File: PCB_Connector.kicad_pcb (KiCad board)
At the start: 2 copper layers, 74.4 x 55.5 mm, 3 parts, among them J1 Conn_01x02_Pin, J2 Conn_01x02_Pin

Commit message: Removing note
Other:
- board text removed: "Align the pins!"
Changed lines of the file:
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@@
     (effects (font (size 4 4) (thickness 1) bold) (justify left bottom))
-  )
-  (gr_text "Align the pins!" (at 145.16 72.32) (layer "Edge.Cuts")
-    (effects (font (size 1 1) (thickness 0.15)) (justify left bottom))
   )
   (segment (start 163.1675 94.2575) (end 164.41 95.5) (width 2) (layer "F.Cu") (net 1))

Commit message: Adding version
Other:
- board text added: "Version: V0.1"
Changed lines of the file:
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@@
     (effects (font (size 4 4) (thickness 1) bold) (justify left bottom))
+  )
+  (gr_text "Version: V0.1" (at 120.65 82.55) (layer "F.SilkS")
+    (effects (font (size 2 2) (thickness 0.3)) (justify left bottom))
   )
   (segment (start 163.1675 94.2575) (end 164.41 95.5) (width 2) (layer "F.Cu") (net 1))

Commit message: Adding PCBWay for a free order :-D
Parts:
- added G***: LOGO, LOGO, F.Cu at (160.7, 81.9)
- added G***: LOGO, LOGO, F.Cu at (161.3, 127.0)

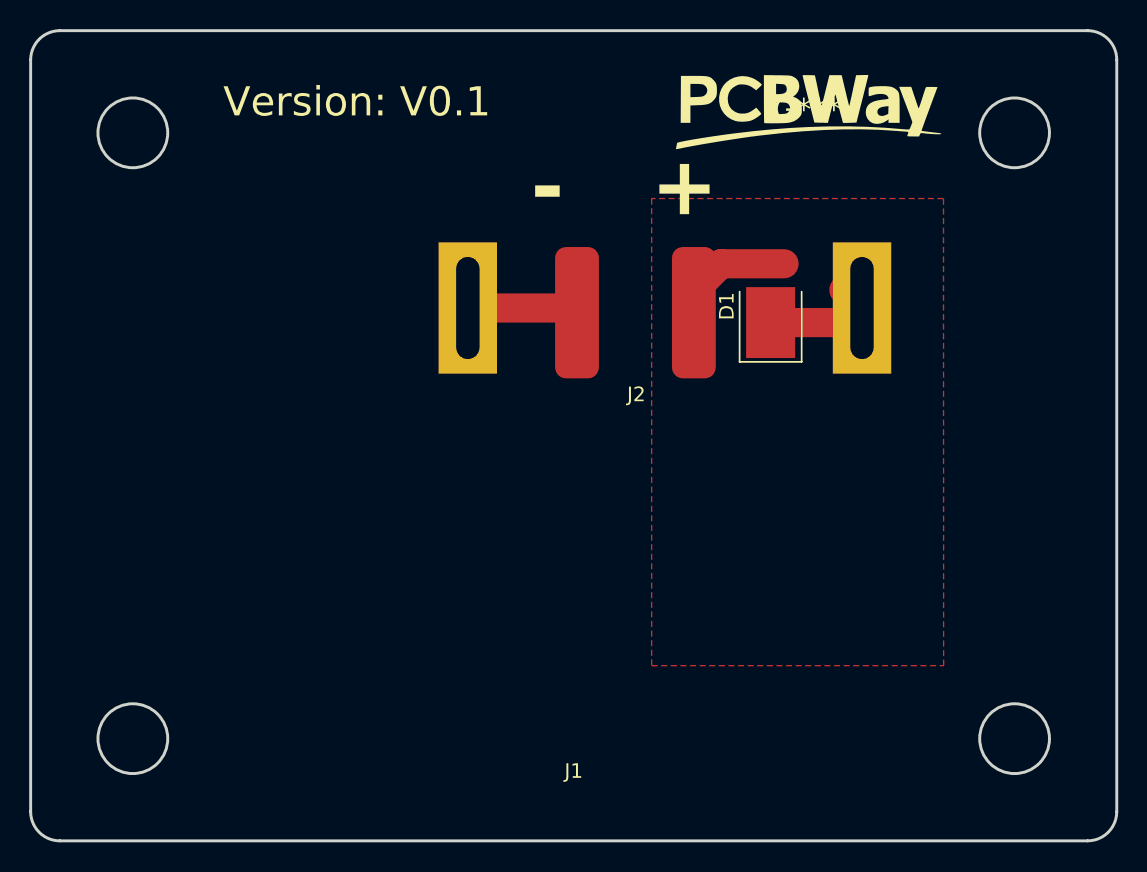
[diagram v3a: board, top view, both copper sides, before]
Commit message: Adding more marking to the PCB and updating image
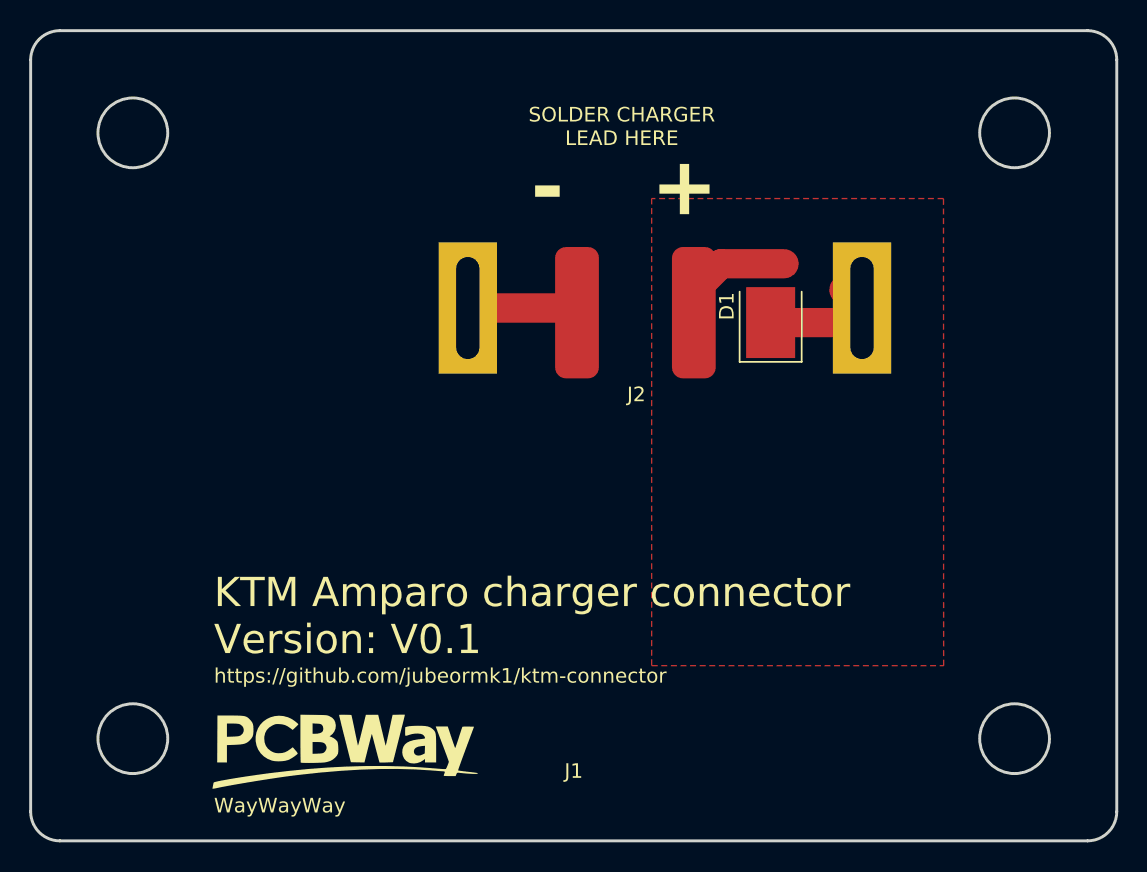
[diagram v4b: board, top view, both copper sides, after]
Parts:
- removed the G*** at (161.3, 127.0)
- moved G*** 54.1 mm to (128.9, 125.7)
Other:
- board text added: "KTM Amparo charger connector Version: V0.1"
- board text added: "SOLDER CHARGER LEAD HERE"
- board text added: "WayWayWay"
- board text added: "https://github.com/jubeormk1/ktm-connector"
- board text removed: "Version: V0.1"
